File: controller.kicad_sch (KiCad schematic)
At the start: 6 parts, among them U1 STM32G071KBTx, U2 MIC5504-3.3YM5

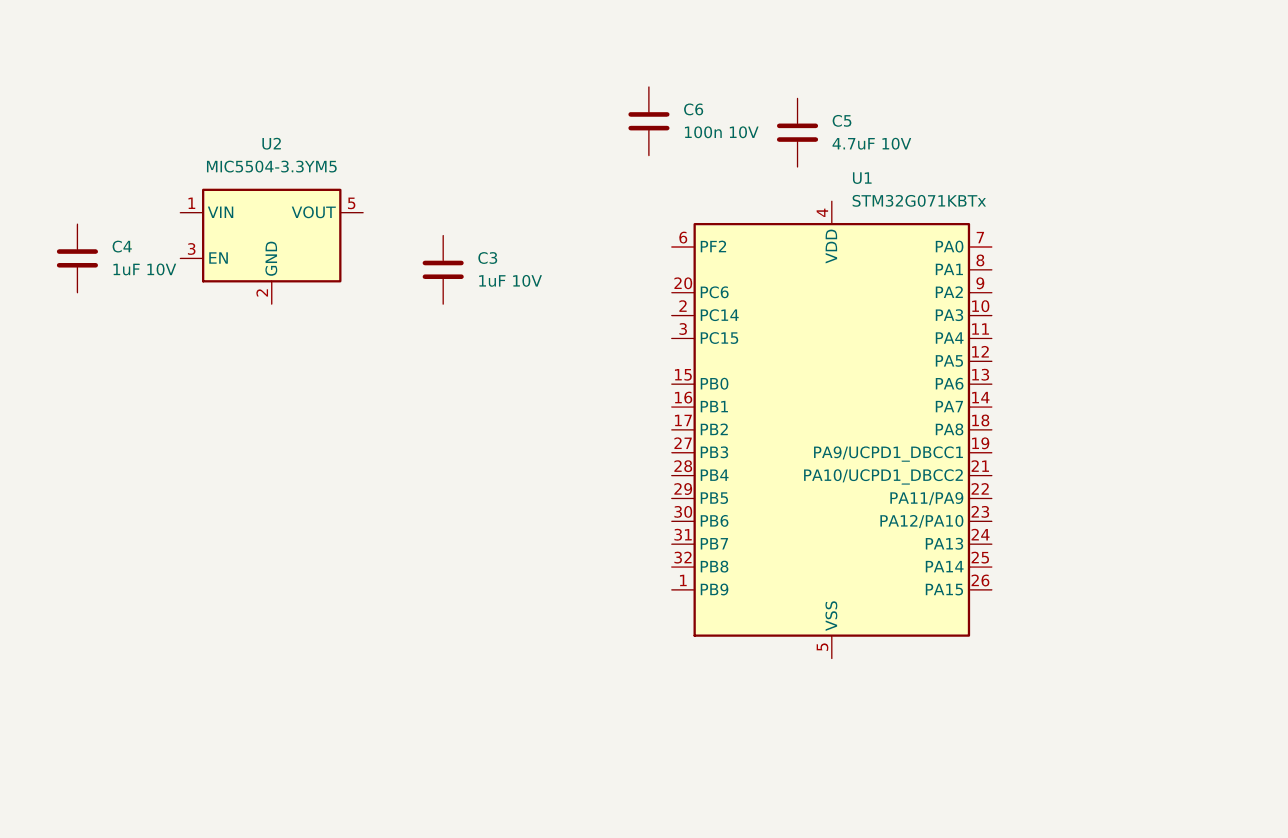
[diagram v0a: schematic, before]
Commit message: assigned footprints
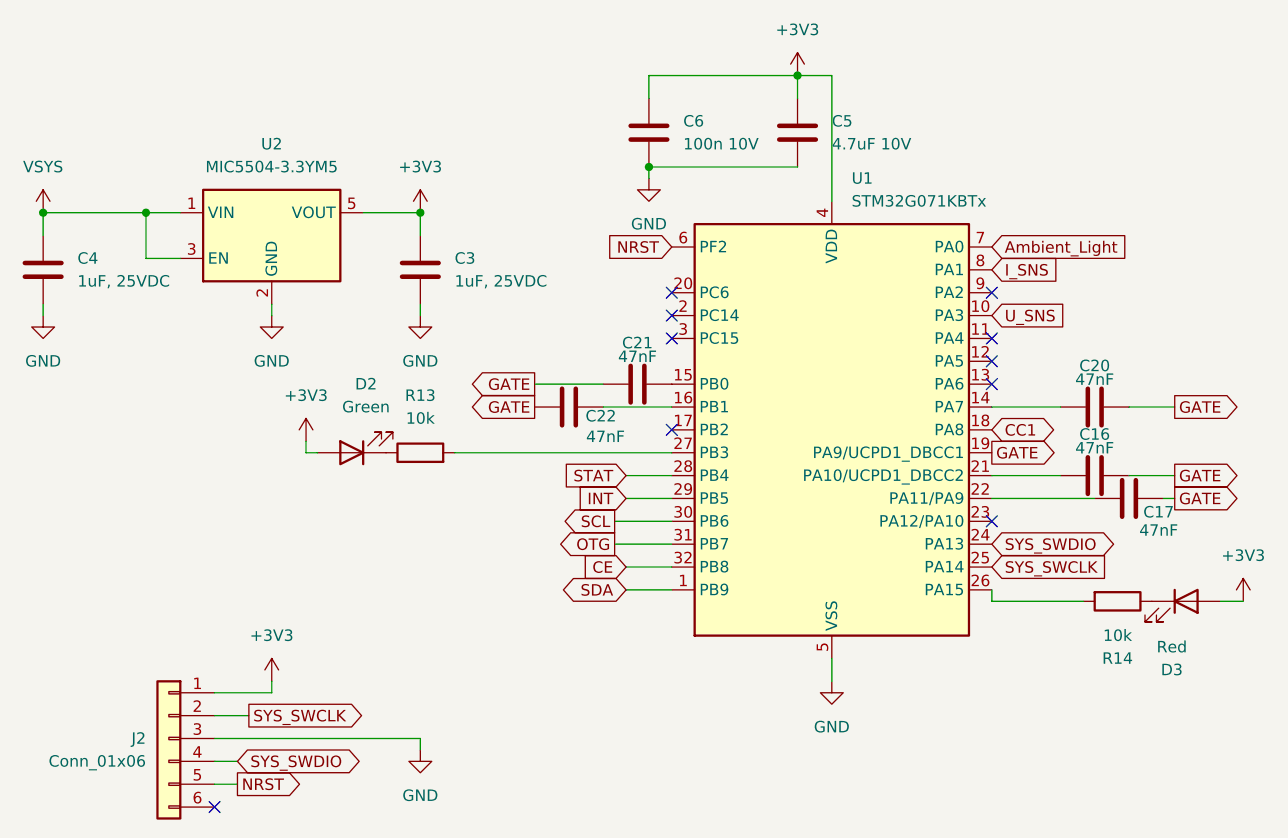
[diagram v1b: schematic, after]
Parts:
- added C16, C17, C20, C21, C22: 47nF, Capacitor_SMD:C_0603_1608Metric_Pad1.08x0.95mm_HandSolder, symbol Device:C
- added D2: Green, LED_SMD:LED_0805_2012Metric, symbol Device:LED
- added D3: Red, LED_SMD:LED_0805_2012Metric_Pad1.15x1.40mm_HandSolder, symbol Device:LED
- added J2: Conn_01x06, Connector_PinHeader_2.54mm:PinHeader_1x06_P2.54mm_Vertical, symbol Connector_Generic:Conn_01x06
- added R13, R14: 10k, Resistor_SMD:R_0603_1608Metric_Pad0.98x0.95mm_HandSolder, symbol Device:R
- C3, C4: value 1uF 10V -> 1uF, 25VDC; footprint (none) -> Capacitor_SMD:C_0603_1608Metric_Pad1.08x0.95mm_HandSolder
- C5, C6: footprint (none) -> Capacitor_SMD:C_0603_1608Metric_Pad1.08x0.95mm_HandSolder
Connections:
- net SDA: now reaches U1.1 (PB9)
- net U_SNS: now reaches U1.10 (PA3)
- net at U1.14 (PA7): now also C20.1
- net at U1.15 (PB0): now also C21.2
- net at U1.16 (PB1): now also C22.2
- net CC1: now reaches U1.18 (PA8)
- net GATE: now reaches U1.19 (PA9/UCPD1_DBCC1)
- net GATE: now also C16.2, C17.2, C20.2, C21.1, C22.1
- net at U1.21 (PA10/UCPD1_DBCC2): now also C16.1
- net at U1.22 (PA11/PA9): now also C17.1
- net SYS_SWDIO: now reaches U1.24 (PA13)
- net SYS_SWDIO: now also J2.4 (Pin_4)
- net SYS_SWCLK: now reaches U1.25 (PA14)
- net SYS_SWCLK: now also J2.2 (Pin_2)
- net at U1.26 (PA15): now also R14.2
- net at U1.27 (PB3): now also R13.2
- net STAT: now reaches U1.28 (PB4)
- net INT: now reaches U1.29 (PB5)
- net SCL: now reaches U1.30 (PB6)
- net OTG: now reaches U1.31 (PB7)
- net CE: now reaches U1.32 (PB8)
- net +3V3: now reaches U1.4 (VDD)
- net +3V3: now also C3.1, C5.1, C6.1, U2.5 (VOUT), D2.2 (A), D3.2 (A), J2.1 (Pin_1)
- net GND: now reaches U1.5 (VSS)
- net GND: now also C3.2, C4.2, C5.2, C6.2, U2.2 (GND), J2.3 (Pin_3)
- net NRST: now reaches U1.6 (PF2)
- net NRST: now also J2.5 (Pin_5)
- net Ambient_Light: now reaches U1.7 (PA0)
- net I_SNS: now reaches U1.8 (PA1)
- net VSYS: now reaches C4.1
- net VSYS: now also U2.1 (VIN), U2.3 (EN)
- new net: D2.1 (K), R13.1
- new net: D3.1 (K), R14.1
- no-connect marks 0 -> 10
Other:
- moved on the sheet: C6

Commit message: Layout begonnen
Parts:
- D2: footprint LED_SMD:LED_0805_2012Metric -> LED_SMD:LED_0805_2012Metric_Pad1.15x1.40mm_HandSolder
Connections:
- net +3V3: no longer D2.2 (A), D3.2 (A)
- net GND: now also D2.1 (K), D3.1 (K)
- net at R13.1: now also D2.2 (A); no longer D2.1 (K)
- net at R14.1: now also D3.2 (A); no longer D3.1 (K)

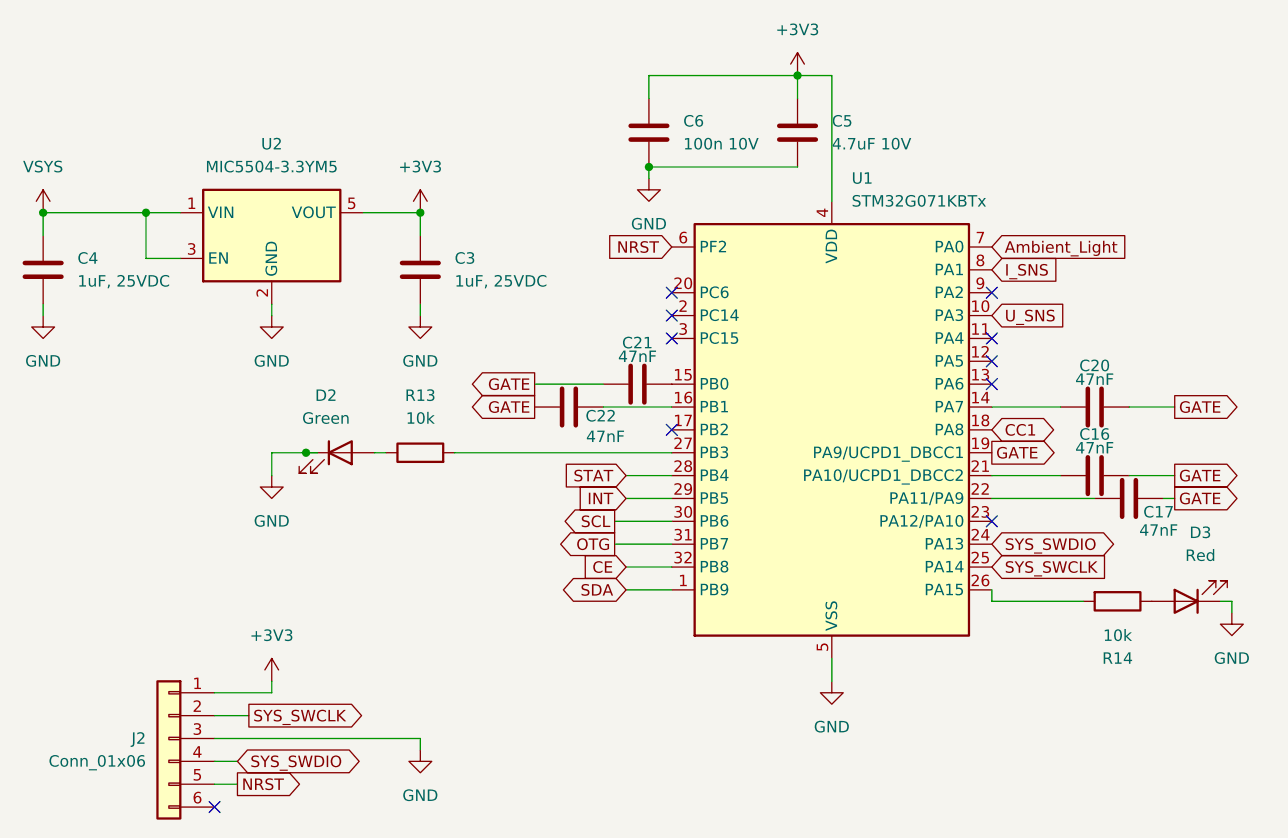
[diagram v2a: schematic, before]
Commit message: marked unused capaacitors as not placed. Pull down on gate channel
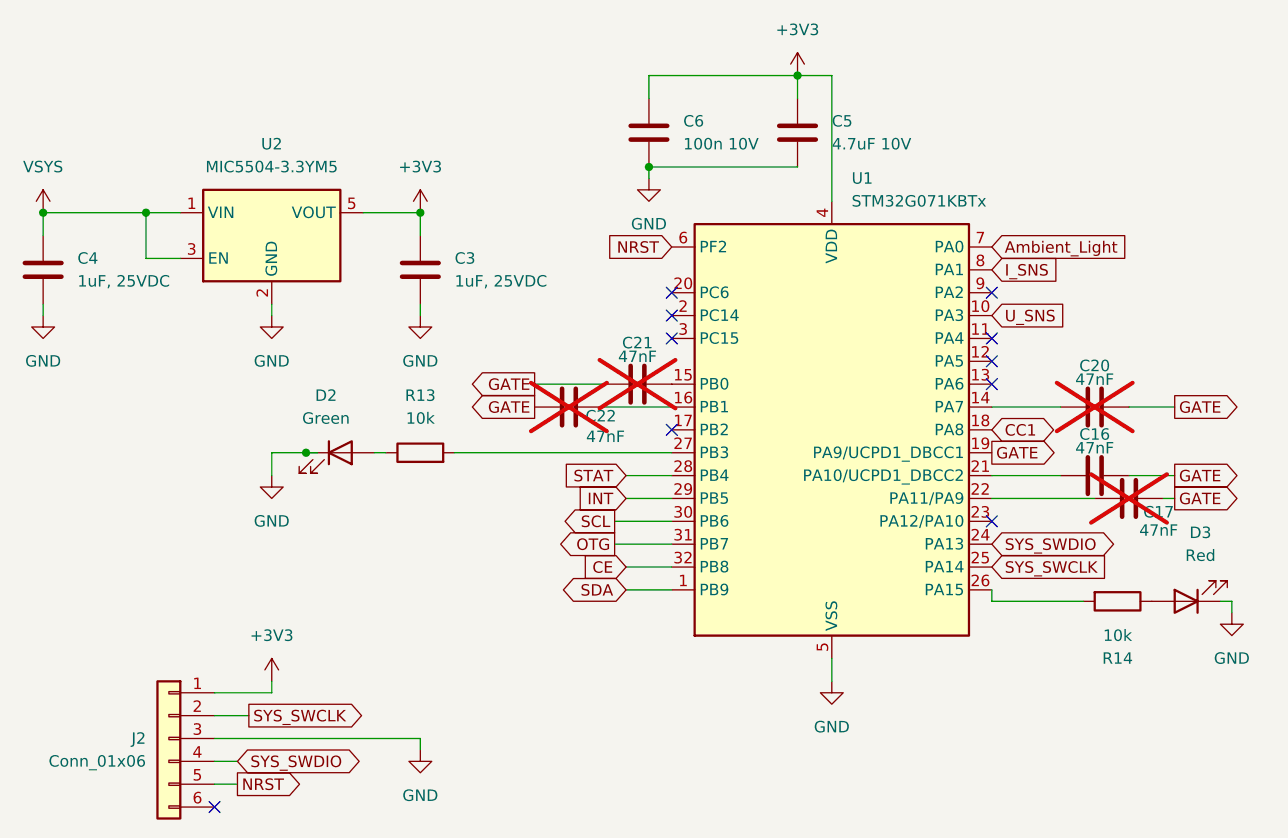
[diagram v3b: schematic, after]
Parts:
- C17, C20, C21, C22: now not fitted
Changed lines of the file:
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@@
 		(in_bom yes)
 		(on_board yes)
-		(dnp no)
+		(dnp yes)
 		(property "Reference" "C22"
 			(at 108.966 78.486 90)
@@
 		(in_bom yes)
 		(on_board yes)
-		(dnp no)
+		(dnp yes)
 		(property "Reference" "C20"
 			(at 163.83 72.898 90)
@@
 		(in_bom yes)
 		(on_board yes)
-		(dnp no)
+		(dnp yes)
 		(property "Reference" "C21"
 			(at 113.03 70.358 90)
@@
 		(in_bom yes)
 		(on_board yes)
-		(dnp no)
+		(dnp yes)
 		(property "Reference" "C17"
 			(at 170.942 89.154 90)
